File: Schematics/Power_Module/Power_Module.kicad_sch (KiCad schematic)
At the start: 34 parts, among them J1 Screw_Terminal_01x02, J2 Screw_Terminal_01x02, J3 Screw_Terminal_01x02, J4 Screw_Terminal_01x02, J6 Stack Male Edge Connector, Q1 PMOS, Q2 PMOS, U1 LMR51430XDDCR, U2 LMR51430XDDCR, U3 LMR51430XDDCR

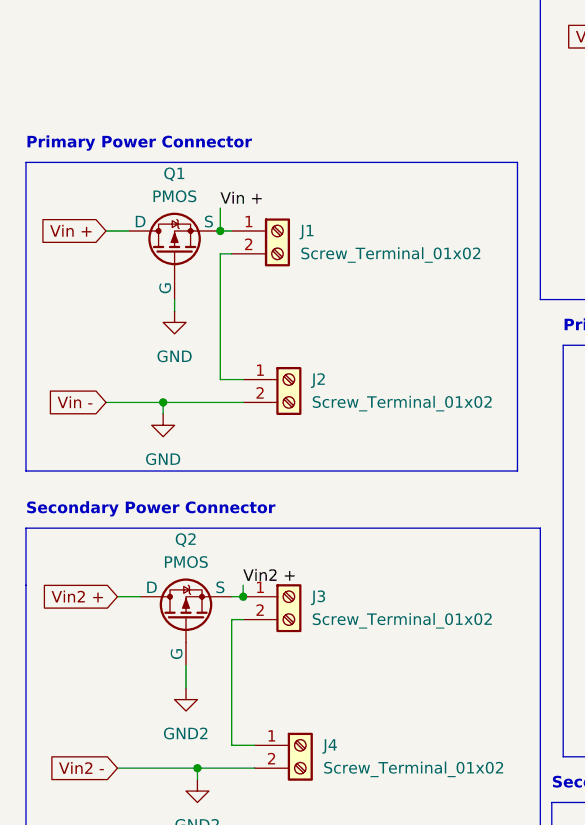
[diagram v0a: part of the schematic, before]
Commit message: Added new P-MOSFETs
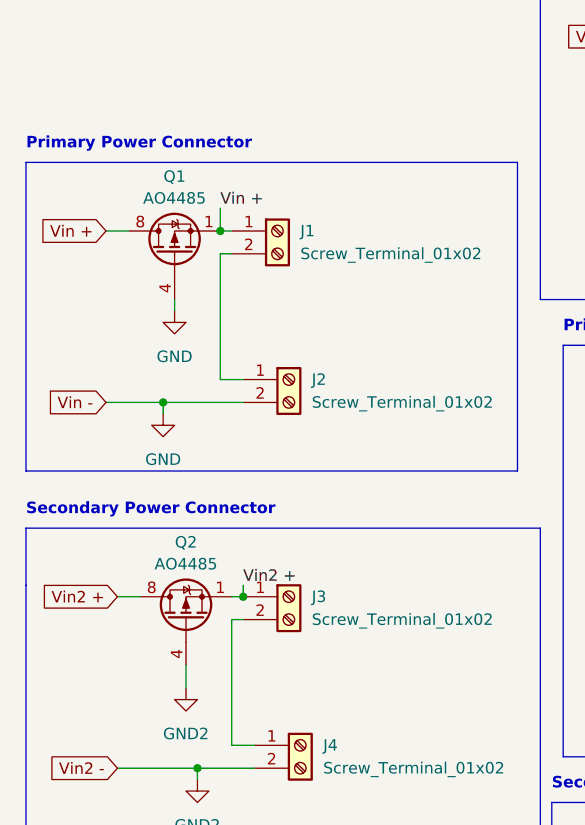
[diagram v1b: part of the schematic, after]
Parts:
- removed Q1, Q2: PMOS, footprints2:YJN3_TEX, symbol Simulation_SPICE:PMOS
- added Q1, Q2: AO4485, Package_SO:SOIC-8_3.9x4.9mm_P1.27mm, symbol Transistor_FET:IRF7404
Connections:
- net GND: now also Q1.4 (G)
- net GND2: now also Q2.4 (G)
- net Vin +: now also Q1.1 (S), Q1.2 (S), Q1.3 (S), Q1.5 (D), Q1.6 (D), Q1.7 (D), Q1.8 (D)
- net Vin 2+: now also Q2.1 (S), Q2.2 (S), Q2.3 (S), Q2.5 (D), Q2.6 (D), Q2.7 (D), Q2.8 (D)

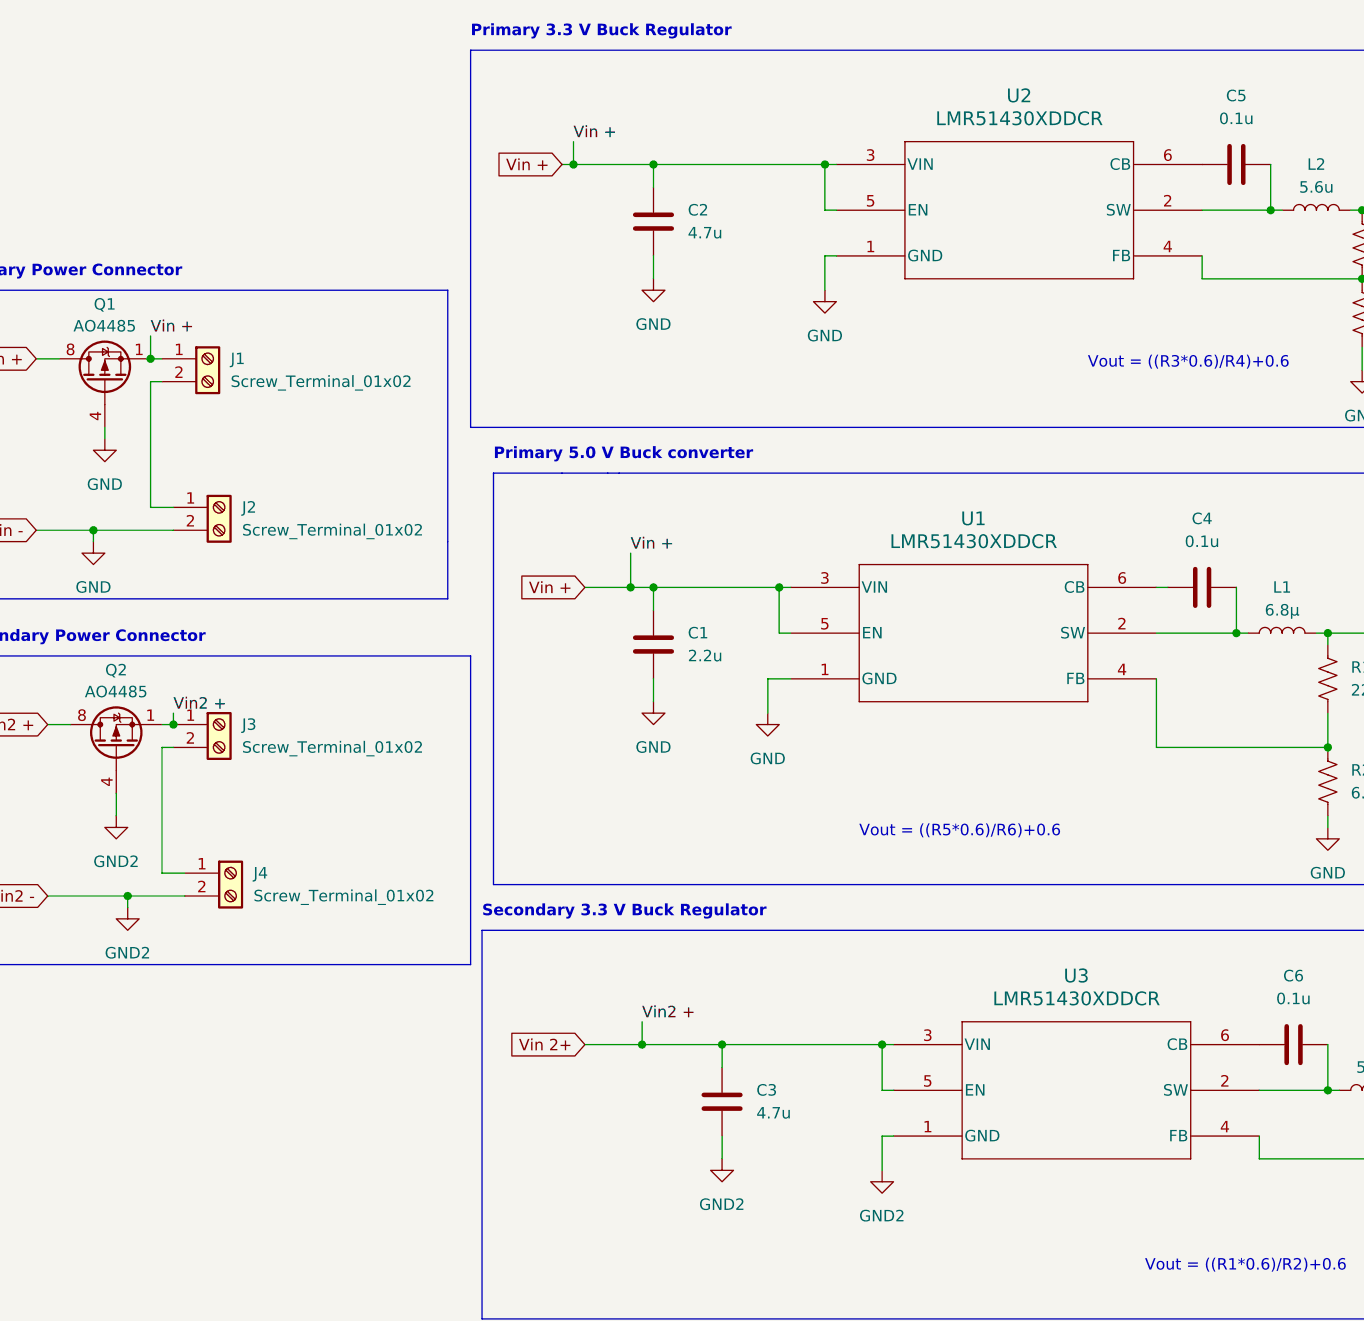
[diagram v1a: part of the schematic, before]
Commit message: Fixed footprints & added proper power connectors
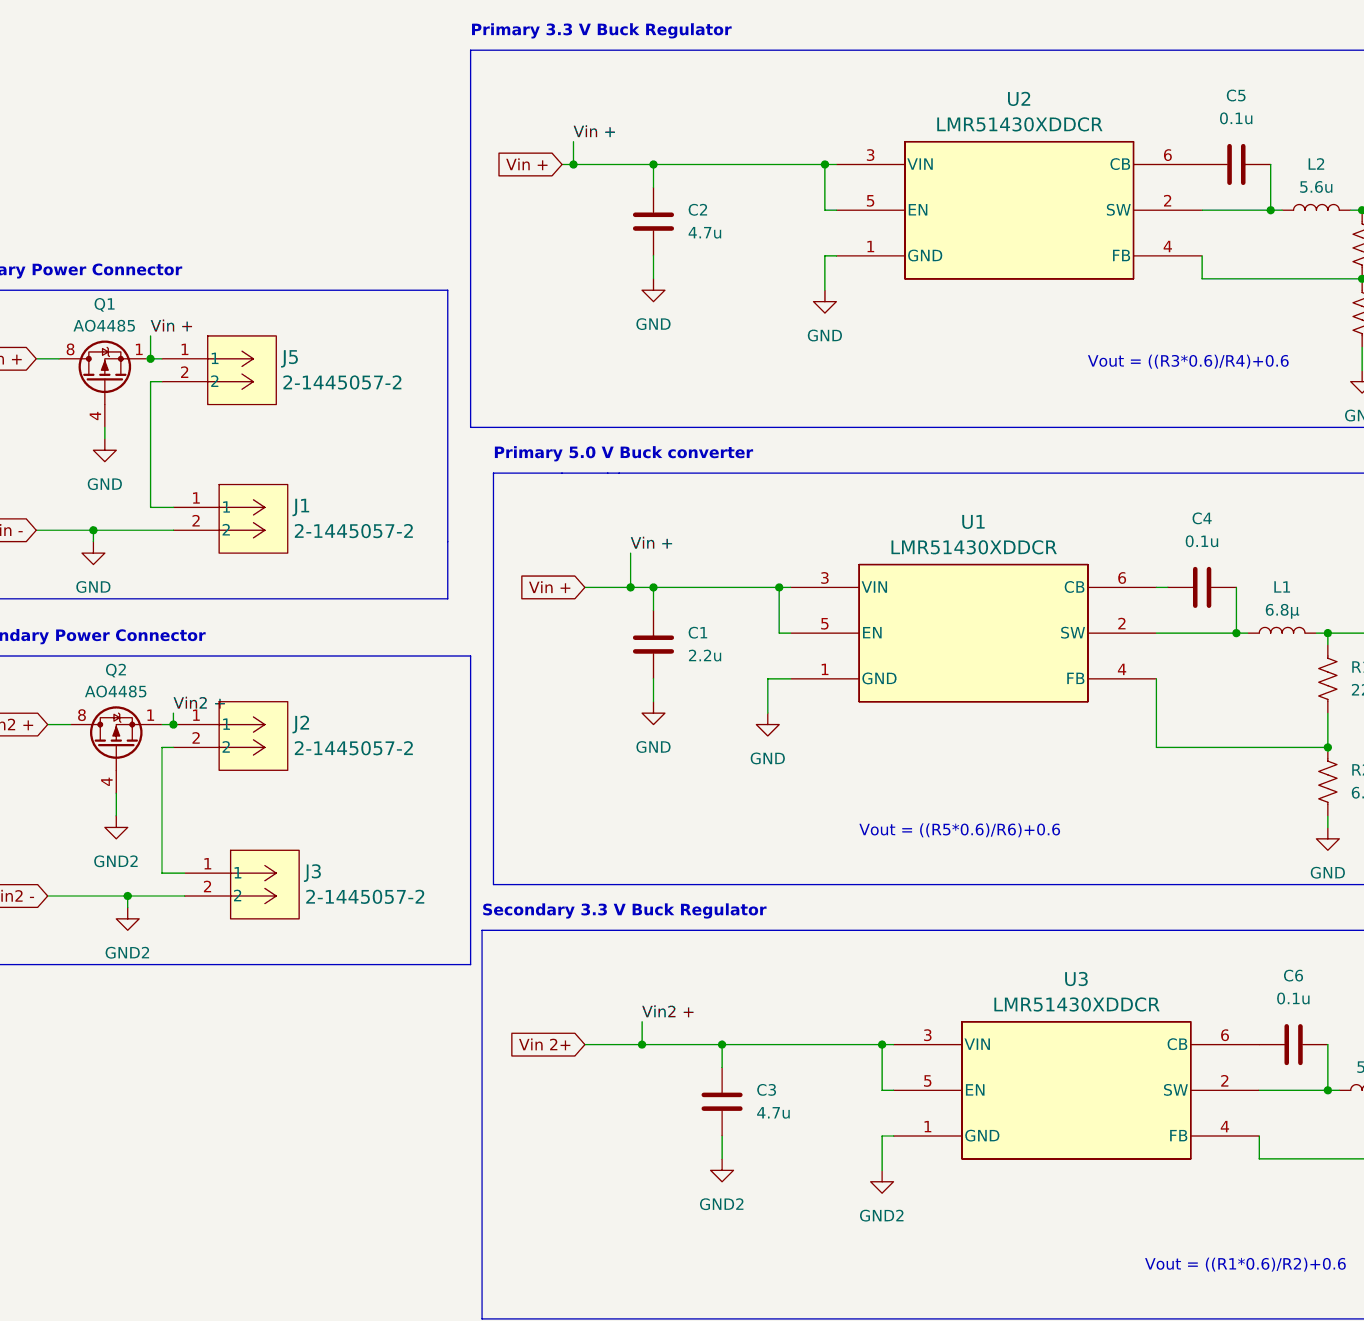
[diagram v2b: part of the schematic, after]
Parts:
- removed J1, J2, J3, J4: Screw_Terminal_01x02, TerminalBlock:TerminalBlock_Altech_AK300-2_P5.00mm, symbol Connector:Screw_Terminal_01x02
- added J1, J2, J3, J5: 2-1445057-2, footprints:CONN_2-1445057-2_TYCO, symbol CONN_2-1445057-2_TYCO:2-1445057-2
- D1, D2, D3: footprint LED_SMD:LED_0201_0603Metric -> LED_SMD:LED_0603_1608Metric
- L1, L2, L3: footprint Inductor_SMD:L_0201_0603Metric -> (none)
- R1, R2, R3, R4, R5, R6, R7, R8, R9: footprint Resistor_SMD:R_0201_0603Metric -> Resistor_SMD:R_0603_1608Metric
- U1, U3: footprint footprints:SOT-23-THIN-6_DDC_TEX -> Package_TO_SOT_SMD:SOT-23-6_Handsoldering
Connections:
- net GND: now also J1.2
- net GND2: now also J3.2
- net Vin +: now also J5.1
- net Vin 2+: now also J2.1
- new net: J2.2, J3.1
- new net: J1.1, J5.2

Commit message: Fixed capacitor footprints
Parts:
- C1, C2, C3, C4, C5, C6, C7, C8, C9: footprint Capacitor_SMD:C_0201_0603Metric -> Capacitor_SMD:C_0603_1608Metric
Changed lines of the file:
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@@
       (effects (font (size 1.27 1.27)) (justify left))
     )
-    (property "Footprint" "Capacitor_SMD:C_0201_0603Metric" (at 93.6752 88.9 0)
+    (property "Footprint" "Capacitor_SMD:C_0603_1608Metric" (at 93.6752 88.9 0)
       (effects (font (size 1.27 1.27)) hide)
     )
@@
       (effects (font (size 1.27 1.27)) (justify left))
     )
-    (property "Footprint" "Capacitor_SMD:C_0201_0603Metric" (at 185.1152 48.26 0)
+    (property "Footprint" "Capacitor_SMD:C_0603_1608Metric" (at 185.1152 48.26 0)
       (effects (font (size 1.27 1.27)) hide)
     )
@@
       (effects (font (size 1.27 1.27)))
     )
-    (property "Footprint" "Capacitor_SMD:C_0201_0603Metric" (at 161.29 30.7848 0)
+    (property "Footprint" "Capacitor_SMD:C_0603_1608Metric" (at 161.29 30.7848 0)
       (effects (font (size 1.27 1.27)) hide)
     )
@@
       (effects (font (size 1.27 1.27)) (justify left))
     )
-    (property "Footprint" "Capacitor_SMD:C_0201_0603Metric" (at 191.4652 146.05 0)
+    (property "Footprint" "Capacitor_SMD:C_0603_1608Metric" (at 191.4652 146.05 0)
       (effects (font (size 1.27 1.27)) hide)
     )
@@
       (effects (font (size 1.27 1.27)) (justify left))
     )
-    (property "Footprint" "Capacitor_SMD:C_0201_0603Metric" (at 101.2952 139.7 0)
+    (property "Footprint" "Capacitor_SMD:C_0603_1608Metric" (at 101.2952 139.7 0)
       (effects (font (size 1.27 1.27)) hide)
     )
@@
       (effects (font (size 1.27 1.27)))
     )
-    (property "Footprint" "Capacitor_SMD:C_0201_0603Metric" (at 157.48 77.7748 0)
+    (property "Footprint" "Capacitor_SMD:C_0603_1608Metric" (at 157.48 77.7748 0)
       (effects (font (size 1.27 1.27)) hide)
     )
@@
       (effects (font (size 1.27 1.27)) (justify left))
     )
-    (property "Footprint" "Capacitor_SMD:C_0201_0603Metric" (at 93.6752 41.91 0)
+    (property "Footprint" "Capacitor_SMD:C_0603_1608Metric" (at 93.6752 41.91 0)
       (effects (font (size 1.27 1.27)) hide)
     )
@@
       (effects (font (size 1.27 1.27)))
     )
-    (property "Footprint" "Capacitor_SMD:C_0201_0603Metric" (at 167.64 128.5748 0)
+    (property "Footprint" "Capacitor_SMD:C_0603_1608Metric" (at 167.64 128.5748 0)
       (effects (font (size 1.27 1.27)) hide)
     )
@@
       (effects (font (size 1.27 1.27)) (justify left))
     )
-    (property "Footprint" "Capacitor_SMD:C_0201_0603Metric" (at 180.0352 95.25 0)
-      (effects (font (size 1.27 1.27)) hide)
-    )
+    (property "Footprint" "Capacitor_SMD:C_0603_1608Metric" (at 180.0352 95.25 0)
+      (effects (font (size 1.27 1.27)) hide)
+    )
